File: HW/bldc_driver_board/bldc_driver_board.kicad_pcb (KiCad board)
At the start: 2 copper layers, 80 x 119.4 mm, 53 parts, among them IC1 DRV8305NPHPR, J1 PWR, J2 N_CN7, J3 N_CN10, J4 HALL, J5 Motor, J6 RJ45, J7 RJ45, Q1 STD140N6F7, Q2 STD140N6F7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

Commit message: -- Added surfaces
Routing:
- net +BATT: track 271.3 -> 121.0 mm, vias 14 -> 47
- net GND: track 343.5 -> 207.1 mm, vias 5 -> 23
- net +5V: track 107.7 -> 37.8 mm, vias 2 -> 1
- net VDD: track 268.5 -> 224.0 mm
- net /GHC: track 50.0 -> 55.5 mm
- net /GHB: track 48.7 -> 50.3 mm
- net /SLC: track 82.3 -> 83.5 mm
- net /SHC: track 51.9 -> 52.7 mm
- net /GLC: track 42.9 -> 43.5 mm
- added copper zone on B.Cu, net +BATT
- added copper zone on F.Cu, net +BATT
- added copper zone on B.Cu, net GND
- added copper zone on F.Cu, net GND
- removed copper zone on F.Cu, net /SHA
- removed copper zone on F.Cu, net /SHB
- removed copper zone on F.Cu, net /SHC

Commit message: -- Added lines to encoder connector
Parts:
- moved J4 1.14 mm to (83.2, 50.0)
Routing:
- net +5V: track 37.8 -> 91.6 mm, vias 1 -> 3
- net VDD: track 224.0 -> 260.6 mm
- net Net-(J4-Pad2): track 4.14 -> 3.00 mm
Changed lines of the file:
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@@
     (thickness 1.6)
     (drawings 4)
-    (tracks 687)
+    (tracks 704)
     (zones 0)
     (modules 53)
@@
   )
   (module Connector_PinHeader_2.54mm:PinHeader_1x05_P2.54mm_Vertical (layer F.Cu)
-    (at 83.185 48.895 270)
+    (at 83.185 50.038 270)
     (descr "Through hole straight pin header, 1x05, 2.54mm pitch, single row")
     (tags "Through hole pin header THT 1x05 2.54mm single row")
@@
   (segment (start 96.299 141.605) (end 100.5355 141.605) (width 0.2032) (layer F.Cu) (net 4))
   (via (at 70.231 53.848) (size 0.635) (drill 0.3048) (layers F.Cu B.Cu) (net 4))
-  (segment (start 73.025 48.895) (end 73.025 51.054) (width 0.2032) (layer F.Cu) (net 4))
-  (segment (start 73.025 51.054) (end 70.231 53.848) (width 0.2032) (layer F.Cu) (net 4))
   (via (at 70.231 56.642) (size 0.635) (drill 0.3048) (layers F.Cu B.Cu) (net 4))
   (segment (start 70.231 53.848) (end 70.231 56.642) (width 0.2032) (layer B.Cu) (net 4))
@@
   (via (at 55.88 164.084) (size 0.635) (drill 0.3048) (layers F.Cu B.Cu) (net 4))
   (via (at 56.642 164.084) (size 0.635) (drill 0.3048) (layers F.Cu B.Cu) (net 4))
+  (segment (start 73.025 52.705) (end 73.025 50.038) (width 0.2032) (layer F.Cu) (net 4))
+  (segment (start 70.231 53.848) (end 71.882 53.848) (width 0.2032) (layer F.Cu) (net 4))
+  (segment (start 71.882 53.848) (end 73.025 52.705) (width 0.2032) (layer F.Cu) (net 4))
   (segment (start 75.2125 112.875) (end 71.783 112.875) (width 0.2032) (layer F.Cu) (net 5))
   (segment (start 71.783 112.875) (end 71.628 113.03) (width 0.2032) (layer F.Cu) (net 5))
@@
   (segment (start 100.5355 140.335) (end 100.838 140.0325) (width 0.2032) (layer F.Cu) (net 18))
   (segment (start 96.299 140.335) (end 100.5355 140.335) (width 0.2032) (layer F.Cu) (net 18))
-  (via (at 38.989 54.61) (size 0.635) (drill 0.3048) (layers F.Cu B.Cu) (net 18))
   (segment (start 73.3575 54.61) (end 71.12 54.61) (width 0.2032) (layer F.Cu) (net 18))
   (segment (start 91.694 56.515) (end 90.4725 56.515) (width 0.2032) (layer F.Cu) (net 18))
@@
   (segment (start 90.4725 52.705) (end 91.694 52.705) (width 0.2032) (layer F.Cu) (net 18))
   (segment (start 91.694 52.705) (end 92.329 53.34) (width 0.2032) (layer F.Cu) (net 18))
-  (segment (start 71.12 54.61) (end 38.989 54.61) (width 0.2032) (layer F.Cu) (net 18))
   (via (at 71.12 54.61) (size 0.635) (drill 0.3048) (layers F.Cu B.Cu) (net 18))
   (via (at 92.329 54.61) (size 0.635) (drill 0.3048) (layers F.Cu B.Cu) (net 18))
@@
   (segment (start 41.656 94.301919) (end 41.656 136.525) (width 0.2032) (layer B.Cu) (net 18))
   (segment (start 41.977919 93.98) (end 41.656 94.301919) (width 0.2032) (layer B.Cu) (net 18))
-  (segment (start 43.18 93.98) (end 41.977919 93.98) (width 0.2032) (layer B.Cu) (net 18))
   (segment (start 42.164 137.033) (end 72.898 137.033) (width 0.2032) (layer B.Cu) (net 18))
+  (segment (start 42.164 93.98) (end 41.91 93.98) (width 0.2032) (layer B.Cu) (net 18))
+  (segment (start 42.164 93.98) (end 41.977919 93.98) (width 0.2032) (layer B.Cu) (net 18))
+  (segment (start 43.18 93.98) (end 42.164 93.98) (width 0.2032) (layer B.Cu) (net 18))
+  (segment (start 41.91 93.98) (end 41.656 93.726) (width 0.2032) (layer B.Cu) (net 18))
+  (via (at 41.656 82.55) (size 0.635) (drill 0.3048) (layers F.Cu B.Cu) (net 18))
+  (segment (start 41.656 93.726) (end 41.656 82.55) (width 0.2032) (layer B.Cu) (net 18))
+  (segment (start 41.656 55.372) (end 42.418 54.61) (width 0.2032) (layer F.Cu) (net 18))
+  (segment (start 41.656 82.55) (end 41.656 55.372) (width 0.2032) (layer F.Cu) (net 18))
+  (segment (start 71.12 54.61) (end 42.418 54.61) (width 0.2032) (layer F.Cu) (net 18))
   (segment (start 85.725 103.5535) (end 87.63 101.6485) (width 0.2032) (layer F.Cu) (net 19))
   (segment (start 85.725 107.188) (end 85.725 103.5535) (width 0.2032) (layer F.Cu) (net 19))
@@
   (segment (start 72.2249 113.4719) (end 72.2249 114.8969) (width 0.2032) (layer B.Cu) (net 49))
   (segment (start 86.36 112.141) (end 89.281 109.22) (width 0.2032) (layer B.Cu) (net 49))
-  (via (at 39.624 48.895) (size 0.635) (drill 0.3048) (layers F.Cu B.Cu) (net 60))
-  (segment (start 75.565 47.692919) (end 75.565 48.895) (width 0.2032) (layer F.Cu) (net 60))
-  (segment (start 75.370081 47.498) (end 75.565 47.692919) (width 0.2032) (layer F.Cu) (net 60))
-  (segment (start 72.009 47.498) (end 75.370081 47.498) (width 0.2032) (layer F.Cu) (net 60))
-  (segment (start 70.612 48.895) (end 72.009 47.498) (width 0.2032) (layer F.Cu) (net 60))
-  (segment (start 39.624 48.895) (end 70.612 48.895) (width 0.2032) (layer F.Cu) (net 60))
+  (segment (start 45.72 109.22) (end 44.45 107.95) (width 0.2032) (layer F.Cu) (net 60))
+  (via (at 44.45 87.376) (size 0.635) (drill 0.3048) (layers F.Cu B.Cu) (net 60))
+  (segment (start 44.45 107.95) (end 44.45 87.376) (width 0.2032) (layer F.Cu) (net 60))
+  (segment (start 44.45 87.376) (end 44.45 84.074) (width 0.2032) (layer B.Cu) (net 60))
+  (via (at 42.926 82.55) (size 0.635) (drill 0.3048) (layers F.Cu B.Cu) (net 60))
+  (segment (start 44.45 84.074) (end 42.926 82.55) (width 0.2032) (layer B.Cu) (net 60))
+  (via (at 42.926 55.626) (size 0.635) (drill 0.3048) (layers F.Cu B.Cu) (net 60))
+  (segment (start 42.926 82.55) (end 42.926 55.626) (width 0.2032) (layer F.Cu) (net 60))
+  (segment (start 75.565 51.943) (end 75.565 50.038) (width 0.2032) (layer B.Cu) (net 60))
+  (segment (start 42.926 55.626) (end 42.926 54.356) (width 0.2032) (layer B.Cu) (net 60))
+  (segment (start 43.18 54.102) (end 68.834 54.102) (width 0.2032) (layer B.Cu) (net 60))
+  (segment (start 68.834 54.102) (end 70.104 52.832) (width 0.2032) (layer B.Cu) (net 60))
+  (segment (start 70.104 52.832) (end 74.676 52.832) (width 0.2032) (layer B.Cu) (net 60))
+  (segment (start 42.926 54.356) (end 43.18 54.102) (width 0.2032) (layer B.Cu) (net 60))
+  (segment (start 74.676 52.832) (end 75.565 51.943) (width 0.2032) (layer B.Cu) (net 60))
   (segment (start 110.49 142.875) (end 96.299 142.875) (width 0.2032) (layer F.Cu) (net 84))
   (segment (start 110.744 101.981) (end 110.744 142.621) (width 0.2032) (layer F.Cu) (net 84))
@@
   (segment (start 96.299 139.065) (end 109.728 139.065) (width 0.2032) (layer F.Cu) (net 86))
   (segment (start 109.728 139.065) (end 110.363 138.43) (width 0.2032) (layer F.Cu) (net 86))
-  (segment (start 83.185 49.9482) (end 83.185 53.0375) (width 0.2032) (layer F.Cu) (net 98))
-  (segment (start 83.185 48.895) (end 83.185 49.9482) (width 0.2032) (layer F.Cu) (net 98))
-  (segment (start 80.645 48.895) (end 80.645 53.0375) (width 0.2032) (layer F.Cu) (net 99))
-  (segment (start 78.105 50.097081) (end 78.105 53.0375) (width 0.2032) (layer F.Cu) (net 100))
-  (segment (start 78.105 48.895) (end 78.105 50.097081) (width 0.2032) (layer F.Cu) (net 100))
+  (segment (start 83.185 49.149) (end 83.185 50.2022) (width 0.2032) (layer F.Cu) (net 98))
+  (segment (start 83.185 50.038) (end 83.185 53.0375) (width 0.2032) (layer F.Cu) (net 98))
+  (segment (start 80.645 51.240081) (end 80.645 53.0375) (width 0.2032) (layer F.Cu) (net 99))
+  (segment (start 80.645 50.038) (end 80.645 51.240081) (width 0.2032) (layer F.Cu) (net 99))
+  (segment (start 78.105 49.149) (end 78.105 50.351081) (width 0.2032) (layer F.Cu) (net 100))
+  (segment (start 78.105 50.038) (end 78.105 53.0375) (width 0.2032) (layer F.Cu) (net 100))
   (segment (start 93.98 152.4) (end 92.075 154.305) (width 0.254) (layer F.Cu) (net 105))
   (segment (start 75.565 154.305) (end 73.66 152.4) (width 0.254) (layer F.Cu) (net 105))
@@
     (polygon
       (pts
-        (xy 91.7575 75.438) (xy 91.821 80.518) (xy 42.926 80.518) (xy 42.8625 75.438)
+        (xy 90.678 75.438) (xy 91.694 76.2) (xy 91.694 79.756) (xy 90.678 80.518) (xy 42.926 80.518)
+        (xy 42.8625 75.438)
       )
     )

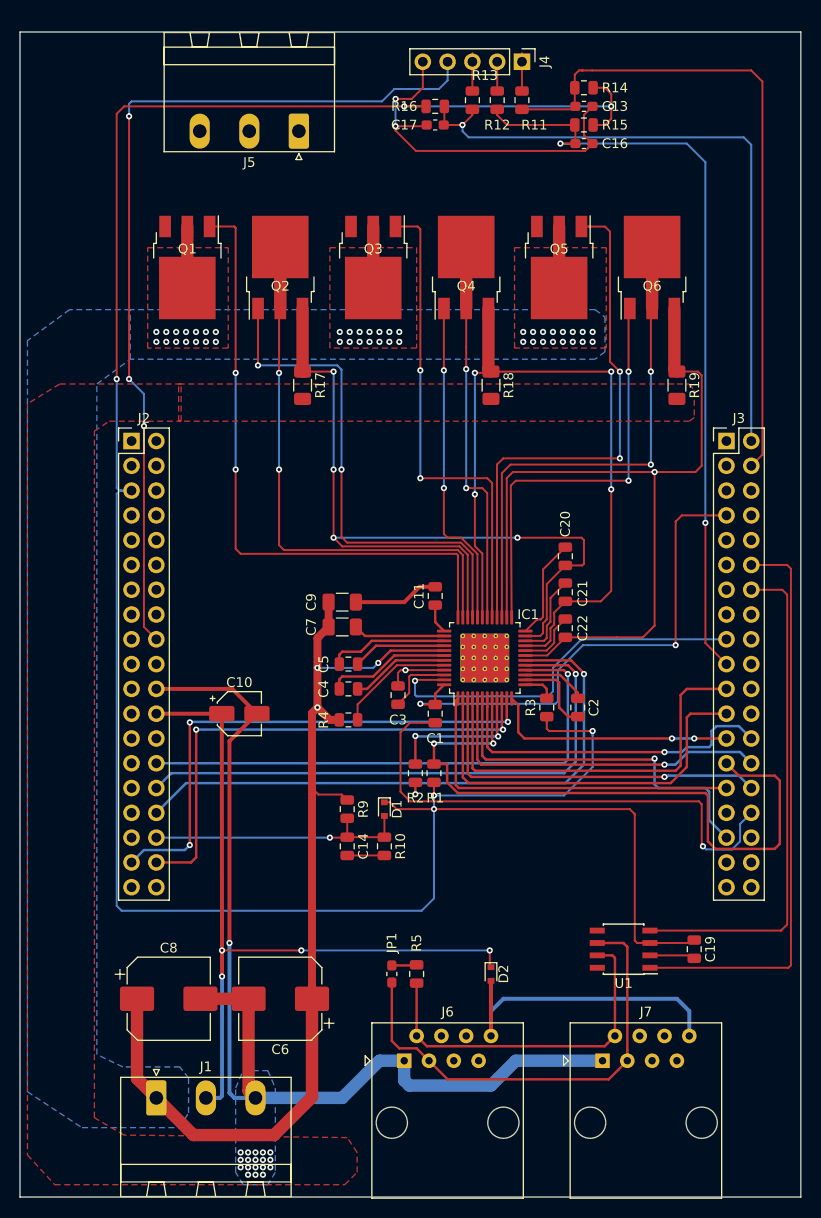
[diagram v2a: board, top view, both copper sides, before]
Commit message: -- Replaced motorconnector and added drill holes
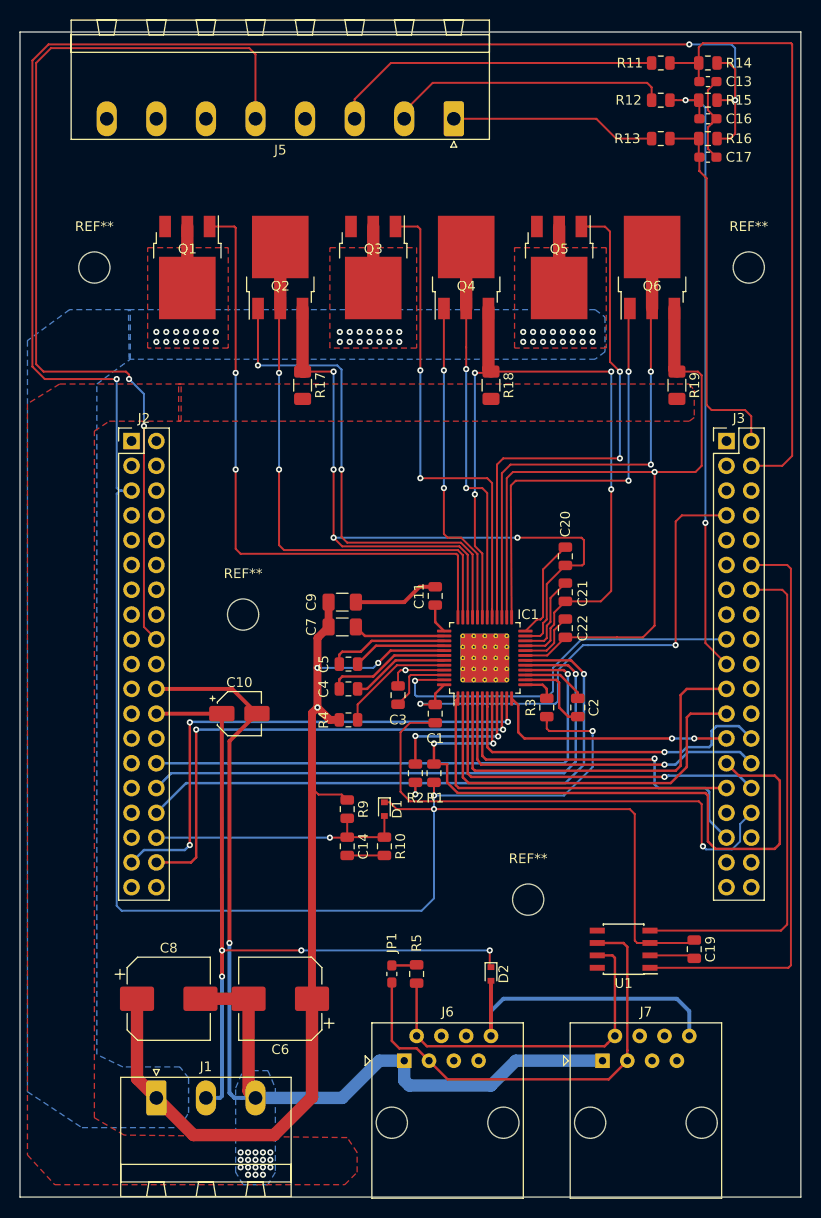
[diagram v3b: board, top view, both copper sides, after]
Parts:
- removed J4: HALL, Connector_PinHeader_2.54mm:PinHeader_1x05_P2.54mm_Vertical
- added REF**: MountingHole_3.2mm_M3, MountingHole:MountingHole_3.2mm_M3, F.Cu at (39.4, 71.1)
- added REF**: MountingHole_3.2mm_M3, MountingHole:MountingHole_3.2mm_M3, F.Cu at (106.4, 71.1)
- added REF**: MountingHole_3.2mm_M3, MountingHole:MountingHole_3.2mm_M3, F.Cu at (83.8, 135.9)
- added REF**: MountingHole_3.2mm_M3, MountingHole:MountingHole_3.2mm_M3, F.Cu at (54.6, 106.7)
- J5: footprint Connector_Phoenix_MSTB:PhoenixContact_MSTBA_2,5_3-G-5,08_1x03_P5.08mm_Horizontal -> Connector_Phoenix_MSTB:PhoenixContact_MSTBA_2,5_8-G-5,08_1x08_P5.08mm_Horizontal
- moved C17 28.1 mm to (102.2, 59.8), turned to 0 degrees
- moved R16 28.1 mm to (102.2, 57.9), turned to 0 degrees
- moved R13 19.7 mm to (97.4, 57.9), turned to 180 degrees
- moved R12 16.8 mm to (97.4, 54.0), turned to 180 degrees
- moved J5 15.9 mm to (76.2, 55.9)
- moved R11 14.7 mm to (97.4, 50.2), turned to 180 degrees
- moved C13 13.0 mm to (102.2, 52.1)
- moved C16 13.0 mm to (102.2, 55.9)
- moved R14 13.0 mm to (102.2, 50.2)
- moved R15 13.0 mm to (102.2, 54.0)
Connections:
- J5 pad 1: /SHC -> /HALL_IN_C
- J5 pad 2: /SHB -> /HALL_IN_B
- J5 pad 3: /SHA -> /HALL_IN_A
- R11 pad 2: Net-(J4-Pad1) -> /HALL_IN_A
- R12 pad 2: Net-(J4-Pad2) -> /HALL_IN_B
- R13 pad 2: Net-(J4-Pad3) -> /HALL_IN_C
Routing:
- net VDD: track 260.6 -> 304.8 mm
- net /HALL_IN_A: track 0.00 -> 34.0 mm
- net GND: track 206.9 -> 178.0 mm, vias 23 -> 21
- net /HALL_IN_B: track 0.00 -> 28.8 mm
- net /HALL_C: track 67.0 -> 38.3 mm, vias 1 -> 0
- net /HALL_IN_C: track 0.00 -> 21.1 mm
- net /HALL_B: track 80.4 -> 65.1 mm
- net +5V: track 91.6 -> 99.1 mm, vias 3 -> 2
- net /HALL_A: track 68.7 -> 63.5 mm
- net Net-(J4-Pad3): track 4.20 -> 0.00 mm
- net Net-(J4-Pad1): track 4.05 -> 0.00 mm
- net Net-(J4-Pad2): track 3.00 -> 0.00 mm
- net /SHB: track 40.6 -> 39.8 mm

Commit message: -- Added thermal pads and connections to UVW
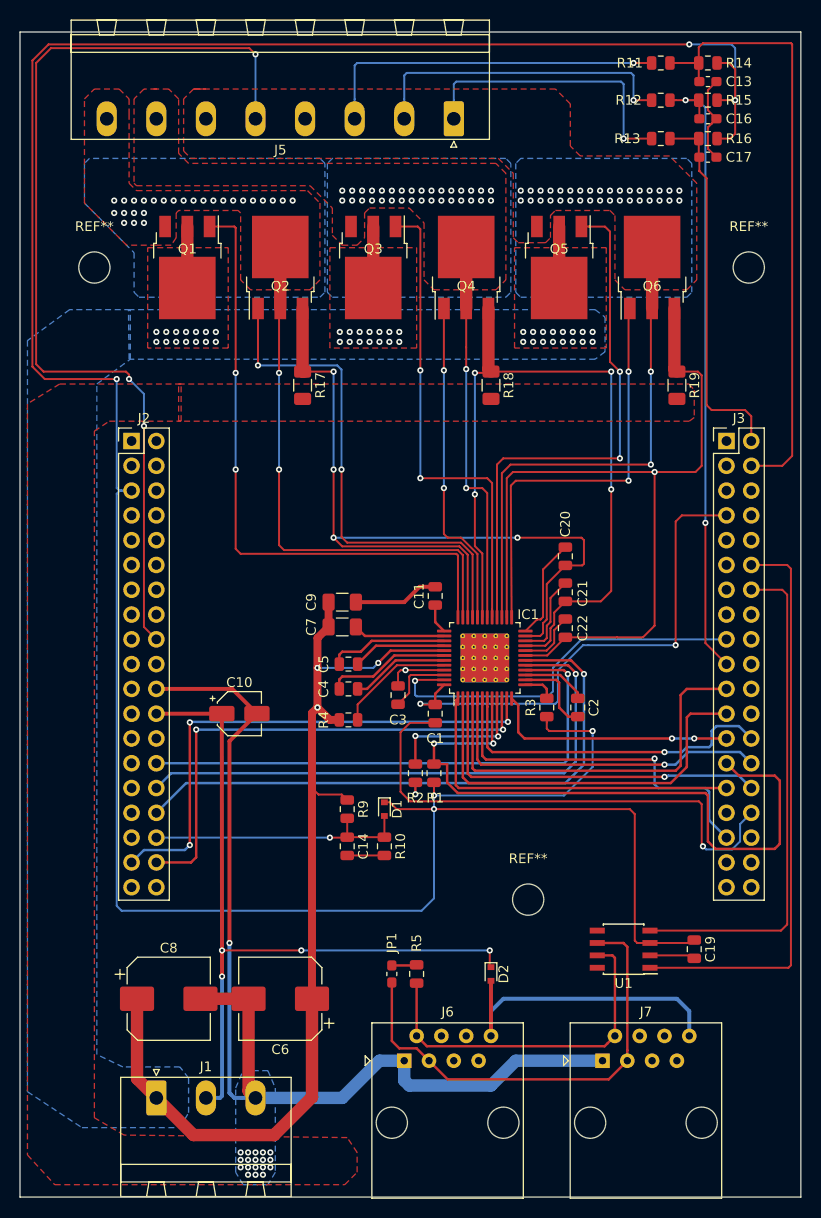
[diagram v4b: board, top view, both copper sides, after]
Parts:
- removed the REF** at (54.6, 106.7)
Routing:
- net /HALL_IN_C: track 21.1 -> 29.6 mm, vias 0 -> 1
- net /HALL_IN_B: track 28.8 -> 33.3 mm, vias 0 -> 1
- net /HALL_IN_A: track 34.0 -> 36.6 mm, vias 0 -> 1
- net /SHC: vias 2 -> 36
- net /SHB: vias 2 -> 34
- net /SHA: vias 2 -> 28
- net +5V: vias 2 -> 3
- added copper zone on B.Cu, net /SHA
- added copper zone on F.Cu, net /SHA
- added copper zone on B.Cu, net /SHB
- added copper zone on F.Cu, net /SHB
- added copper zone on B.Cu, net /SHC
- added copper zone on F.Cu, net /SHC
